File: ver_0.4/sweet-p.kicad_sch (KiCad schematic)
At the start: 39 parts, among them J10 Micro_SD_Card, J2 Screw_Terminal_01x02, J3 Conn_01x04_Female, J4 Conn_01x04_Female, J5 Screw_Terminal_01x05, J7 Conn_01x06_Pin, U1 adafruit_tpl511x, U4 ssd1306, U7 ds3231, U8 P78A05-1000

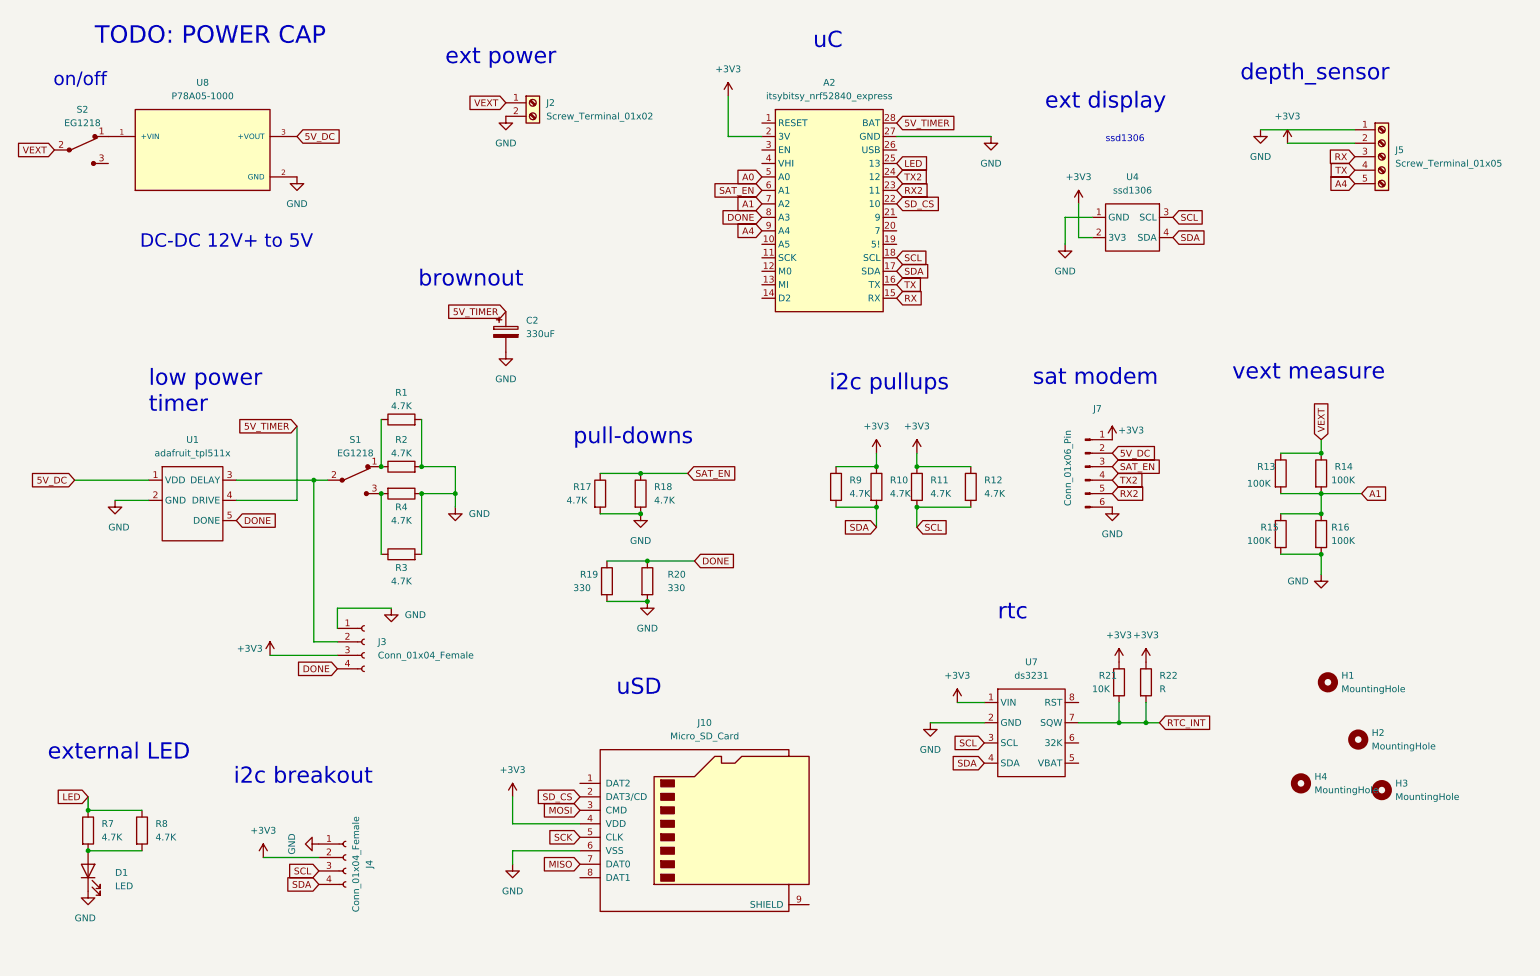
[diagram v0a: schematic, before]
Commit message: pin assignments and initial layout for ver 0.4
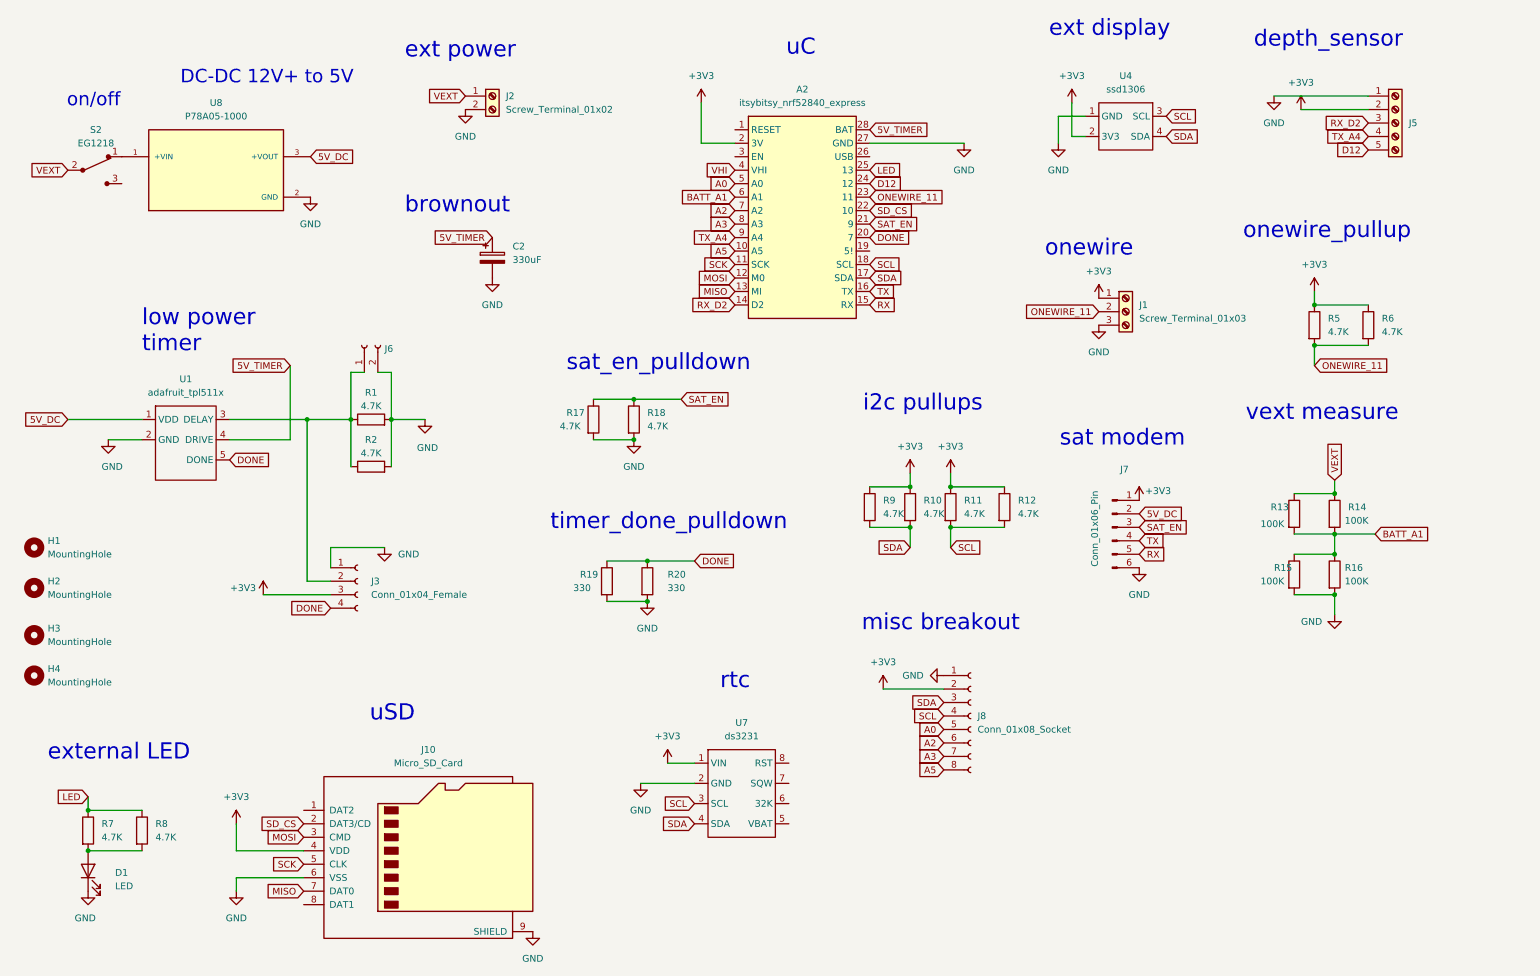
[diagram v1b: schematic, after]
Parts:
- removed J4: Conn_01x04_Female, Connector_PinSocket_2.54mm:PinSocket_1x04_P2.54mm_Vertical, symbol Connector:Conn_01x04_Female
- removed R21: 10K, Resistor_SMD:R_0603_1608Metric_Pad0.98x0.95mm_HandSolder, symbol Device:R
- removed R22: R, Resistor_THT:R_Axial_DIN0204_L3.6mm_D1.6mm_P7.62mm_Horizontal, symbol Device:R
- removed R3: 4.7K, Resistor_SMD:R_0603_1608Metric_Pad0.98x0.95mm_HandSolder, symbol Device:R
- removed R4: 4.7K, Resistor_THT:R_Axial_DIN0204_L3.6mm_D1.6mm_P7.62mm_Horizontal, symbol Device:R
- removed S1: EG1218, digikey-footprints:Switch_Slide_11.6x4mm_EG1218, symbol dk_Slide-Switches:EG1218
- added J1: Screw_Terminal_01x03, TerminalBlock_Phoenix:TerminalBlock_Phoenix_MKDS-1,5-3_1x03_P5.00mm_Horizontal, symbol Connector:Screw_Terminal_01x03
- added J6: Conn_01x02_Socket, Connector_PinSocket_2.54mm:PinSocket_1x02_P2.54mm_Vertical, symbol Connector:Conn_01x02_Socket
- added J8: Conn_01x08_Socket, Connector_PinSocket_2.54mm:PinSocket_1x08_P2.54mm_Vertical, symbol Connector:Conn_01x08_Socket
- added R5: 4.7K, Resistor_SMD:R_0603_1608Metric_Pad0.98x0.95mm_HandSolder, symbol Device:R
- added R6: 4.7K, Resistor_THT:R_Axial_DIN0204_L3.6mm_D1.6mm_P7.62mm_Horizontal, symbol Device:R
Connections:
- net +3V3: now also J1.1 (Pin_1), J8.2 (Pin_2), R5.1, R6.1
- net A0: now also J8.5 (Pin_5)
- net DONE: now also A2.20 (7); no longer A2.8 (A3)
- net GND: now also J10.9 (SHIELD), J1.3 (Pin_3), J6.2 (Pin_2), J8.1 (Pin_1)
- net MISO: now also A2.13 (MI)
- net MOSI: now also A2.12 (M0)
- net RX: now also J7.5 (Pin_5); no longer J5.3 (Pin_3)
- net SAT_EN: now also A2.21 (9); no longer A2.6 (A1)
- net SCK: now also A2.11 (SCK)
- net SCL: now also J8.4 (Pin_4)
- net SDA: now also J8.3 (Pin_3)
- net TX: now also J7.4 (Pin_4); no longer J5.4 (Pin_4)
- net at J3.2 (Pin_2), U1.3 (DELAY): now also R1.1, R2.1, J6.1 (Pin_1)
- net A5: now reaches A2.10 (A5)
- net A5: now also J8.8 (Pin_8)
- net RX_D2: now reaches A2.14 (D2)
- net RX_D2: now also J5.3 (Pin_3)
- net VHI: now reaches A2.4 (VHI)
- net A1 renamed BATT_A1
- net BATT_A1: now also A2.6 (A1); no longer A2.7 (A2)
- net A4 renamed D12
- net D12: now also A2.24 (12); no longer A2.9 (A4)
- net RTC_INT: no longer names the net of U7.7 (SQW)
- net RX2 renamed ONEWIRE_11
- net ONEWIRE_11: now also J1.2 (Pin_2), R5.2, R6.2; no longer J7.5 (Pin_5)
- removed net TX2: A2.24 (12), J7.4 (Pin_4)
- new net A2: A2.7 (A2), J8.6 (Pin_6)
- new net A3: A2.8 (A3), J8.7 (Pin_7)
- new net TX_A4: A2.9 (A4), J5.4 (Pin_4)
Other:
- note added: "misc breakout"
- note added: "onewire"
- note added: "onewire_pullup"
- note added: "sat_en_pulldown"
- note added: "timer_done_pulldown"
- note removed: "TODO: POWER CAP"
- note removed: "i2c breakout"
- note removed: "pull-downs"
- note removed: "ssd1306"
- moved on the sheet: A2, C2, J10, J2, J3, J5, J7, R1, R10, R11, R12, R13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
